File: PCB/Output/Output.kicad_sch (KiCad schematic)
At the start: 62 parts, among them J1 POWER, J10 O7, J11 O8, J12 O9, J13 O10, J2 Shelly, J2 USB-C, J4 O1, J5 O2, J6 O3, J7 O4, J8 O5, J9 O6, U1 MD8942, U2 ESP32-S3-MINI-1, U3 ISL89410, U4 ISL89410, U5 ISL89410, U6 ISL89410, U7 ISL89410

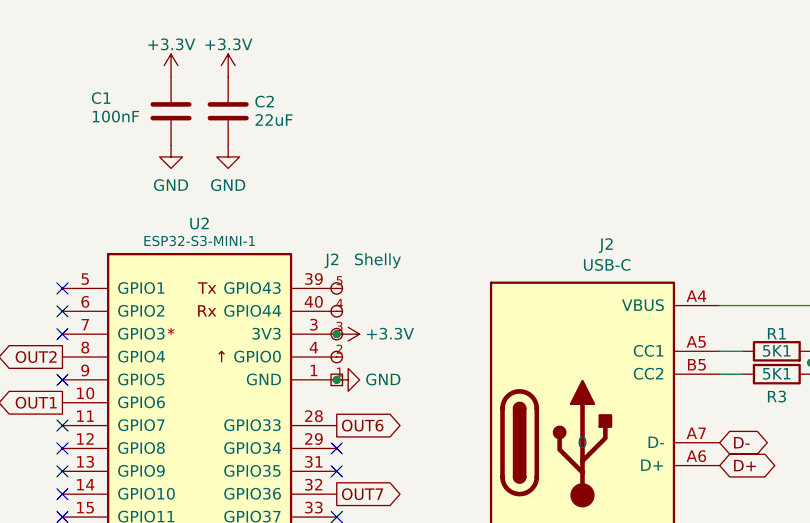
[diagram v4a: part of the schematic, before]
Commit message: Reworked boarder, and added simple LED on GPIO 0
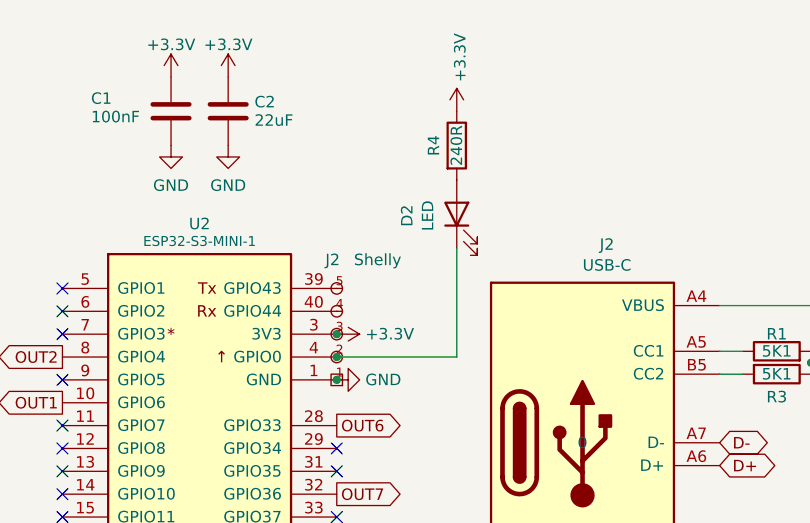
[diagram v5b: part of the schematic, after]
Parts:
- added D2: LED, LED_SMD:LED_0402_1005Metric, symbol Device:LED
- added R4: 240R, RevK:R_0402, symbol Device:R
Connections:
- net +3.3V: now also R4.1
- net at J2.2 (0), U2.4 (GPIO0): now also D2.1 (K)
- new net: D2.2 (A), R4.2
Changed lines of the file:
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@@
   (junction (at 95.885 87.63) (diameter 0) (color 0 0 0 0)
   )
+  (junction (at 68.58 55.245) (diameter 0) (color 0 0 0 0)
+  )
   (junction (at 68.58 57.785) (diameter 0) (color 0 0 0 0)
   )
@@
     (stroke (width 0) (type default))
   )
+  (wire (pts (xy 68.58 55.245) (xy 81.915 55.245))
+    (stroke (width 0) (type default))
+  )
   (wire (pts (xy 126.365 55.88) (xy 121.285 55.88))
     (stroke (width 0) (type default))
   )
+  (wire (pts (xy 81.915 55.245) (xy 81.915 43.18))
+    (stroke (width 0) (type default))
+  )
   (wire (pts (xy 111.125 54.61) (xy 113.665 54.61))
     (stroke (width 0) (type default))
@@
     )
   )
+  (symbol (lib_id "power:+3.3V") (at 81.915 27.94 0) (unit 1)
+    (in_bom yes) (on_board yes) (dnp no)
+    (property "Reference" "#PWR022" (at 81.915 31.75 0)
+      (effects (font (size 1.27 1.27)) hide)
+    )
+    (property "Value" "+3.3V" (at 82.296 24.6888 90)
+      (effects (font (size 1.27 1.27)) (justify left))
+    )
+    (property "Footprint" "" (at 81.915 27.94 0)
+      (effects (font (size 1.27 1.27)) hide)
+    )
+    (property "Datasheet" "" (at 81.915 27.94 0)
+      (effects (font (size 1.27 1.27)) hide)
+    )
+    (pin "1")
+    (instances
+      (project "GenericS3"
+        (path "/2d210a96-f81f-42a9-8bf4-1b43c11086f3"
+          (reference "#PWR022") (unit 1)
+        )
+      )
+      (project "Tas"
+        (path "/42713045-fffd-4b2d-ae1e-7232d705fb12"
+          (reference "#PWR021") (unit 1)
+        )
+      )
+      (project "Output"
+        (path "/770ad51a-7219-4633-b24a-bd20feb0a6c5"
+          (reference "#PWR083") (unit 1)
+        )
+      )
+    )
+  )
   (symbol (lib_id "power:GND") (at 48.895 177.165 180) (unit 1)
     (in_bom yes) (on_board yes) (dnp no) (fields_autoplaced)
@@
     )
   )
+  (symbol (lib_id "Device:LED") (at 81.915 39.37 90) (unit 1)
+    (in_bom yes) (on_board yes) (dnp no)
+    (property "Reference" "D2" (at 76.4032 39.5478 0)
+      (effects (font (size 1.27 1.27)))
+    )
+    (property "Value" "LED" (at 78.7146 39.5478 0)
+      (effects (font (size 1.27 1.27)))
+    )
+    (property "Footprint" "LED_SMD:LED_0402_1005Metric" (at 81.915 39.37 0)
+      (effects (font (size 1.27 1.27)) hide)
+    )
+    (property "Datasheet" "~" (at 81.915 39.37 0)
+      (effects (font (size 1.27 1.27)) hide)
+    )
+    (property "LCSC Part #" "C965790" (at 81.915 39.37 0)
+      (effects (font (size 1.27 1.27)) hide)
+    )
+    (pin "1")
+    (pin "2")
+    (instances
+      (project "GenericS3"
+        (path "/2d210a96-f81f-42a9-8bf4-1b43c11086f3"
+          (reference "D2") (unit 1)
+        )
+      )
+      (project "Tas"
+        (path "/42713045-fffd-4b2d-ae1e-7232d705fb12"
+          (reference "D3") (unit 1)
+        )
+      )
+      (project "Output"
+        (path "/770ad51a-7219-4633-b24a-bd20feb0a6c5"
+          (reference "D13") (unit 1)
+        )
+      )
+    )
+  )
   (symbol (lib_id "power:+3.3V") (at 79.375 184.785 180) (unit 1)
     (in_bom yes) (on_board yes) (dnp no) (fields_autoplaced)
@@
         )
       )
+    )
+  )
+  (symbol (lib_id "Device:R") (at 81.915 31.75 0) (unit 1)
+    (in_bom yes) (on_board yes) (dnp no)
+    (property "Reference" "R4" (at 79.375 31.75 90)
+      (effects (font (size 1.27 1.27)))
+    )
+    (property "Value" "240R" (at 81.915 31.75 90)
+      (effects (font (size 1.27 1.27)))
+    )
+    (property "Footprint" "RevK:R_0402" (at 80.137 31.75 90)
+      (effects (font (size 1.27 1.27)) hide)
+    )
+    (property "Datasheet" "~" (at 81.915 31.75 0)
+      (effects (font (size 1.27 1.27)) hide)
+    )
+    (pin "1")
+    (pin "2")
+    (instances
+      (project "GenericS3"
+        (path "/2d210a96-f81f-42a9-8bf4-1b43c11086f3"
+          (reference "R4") (unit 1)
+        )
+      )
+      (project "Tas"
+        (path "/42713045-fffd-4b2d-ae1e-7232d705fb12"
+          (reference "R5") (unit 1)
+        )
+      )
+      (project "Output"
+        (path "/770ad51a-7219-4633-b24a-bd20feb0a6c5"
+          (reference "R7") (unit 1)
+        )
+      )

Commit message: Library update
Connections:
- net +3.3V: now also D1.3 (-), D1.3 (-), D1.3 (-), D1.3 (-), D1.3 (-), D1.3 (-), D1.3 (-), D1.3 (-), D1.3 (-), D1.3 (-), D1.3 (-); no longer D1.2 (+), D1.2 (+), D1.2 (+), D1.2 (+), D1.2 (+), D1.2 (+), D1.2 (+), D1.2 (+), D1.2 (+), D1.2 (+), D1.2 (+)
- net GND: now also D1.2 (+), D1.2 (+), D1.2 (+), D1.2 (+), D1.2 (+), D1.2 (+), D1.2 (+), D1.2 (+), D1.2 (+), D1.2 (+), D1.2 (+); no longer D1.3 (⏚), D1.3 (⏚), D1.3 (⏚), D1.3 (⏚), D1.3 (⏚), D1.3 (⏚), D1.3 (⏚), D1.3 (⏚), D1.3 (⏚), D1.3 (⏚), D1.3 (⏚)
- net RGB renamed LED
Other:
- moved on the sheet: C3, R1
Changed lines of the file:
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@@
   (junction (at 68.58 52.705) (diameter 0) (color 0 0 0 0)
   )
-  (junction (at 79.375 102.235) (diameter 0) (color 0 0 0 0)
+  (junction (at 79.375 101.6) (diameter 0) (color 0 0 0 0)
   )
   (junction (at 121.285 55.88) (diameter 0) (color 0 0 0 0)
@@
   (no_connect (at 38.1 73.025))
   (no_connect (at 38.1 52.705))
-  (no_connect (at 38.1 102.235))
+  (no_connect (at 113.665 180.975))
   (no_connect (at 38.1 65.405))
   (no_connect (at 38.1 90.805))
@@
     (stroke (width 0) (type default))
   )
-  (wire (pts (xy 68.58 102.235) (xy 79.375 102.235))
+  (wire (pts (xy 68.58 101.6) (xy 79.375 101.6))
     (stroke (width 0) (type default))
   )
@@
     )
   )
-  (global_label "RGB" (shape input) (at 25.4 180.975 180) (fields_autoplaced)
+  (global_label "LED" (shape input) (at 25.4 180.975 180) (fields_autoplaced)
     (effects (font (size 1.27 1.27)) (justify right))
-    (property "Intersheetrefs" "${INTERSHEET_REFS}" (at 19.259 180.975 0)
+    (property "Intersheetrefs" "${INTERSHEET_REFS}" (at 19.6219 180.975 0)
       (effects (font (size 1.27 1.27)) (justify right) hide)
     )
@@
     )
   )
-  (global_label "RGB" (shape output) (at 38.1 88.265 180) (fields_autoplaced)
+  (global_label "LED" (shape output) (at 38.1 88.265 180) (fields_autoplaced)
     (effects (font (size 1.27 1.27)) (justify right))
-    (property "Intersheetrefs" "${INTERSHEET_REFS}" (at 31.959 88.265 0)
+    (property "Intersheetrefs" "${INTERSHEET_REFS}" (at 32.3219 88.265 0)
       (effects (font (size 1.27 1.27)) (justify right) hide)
     )
@@
       (effects (font (size 1.27 1.27)) hide)
     )
+    (property "Part No" "" (at 255.905 32.385 0)
+      (effects (font (size 1.27 1.27)) hide)
+    )
+    (property "Note" "" (at 255.905 32.385 0)
+      (effects (font (size 1.27 1.27)) hide)
+    )
     (pin "~")
     (instances
@@
       (effects (font (size 1.27 1.27)) hide)
     )
+    (property "Part No" "" (at 255.905 30.48 0)
+      (effects (font (size 1.27 1.27)) hide)
+    )
+    (property "Note" "" (at 255.905 30.48 0)
+      (effects (font (size 1.27 1.27)) hide)
+    )
     (pin "~")
     (instances
@@
     )
   )
-  (symbol (lib_id "Device:C") (at 79.375 106.045 0) (unit 1)
+  (symbol (lib_id "Device:C") (at 79.375 105.41 0) (unit 1)
     (in_bom yes) (on_board yes) (dnp no) (fields_autoplaced)
-    (property "Reference" "C3" (at 82.296 105.2103 0)
+    (property "Reference" "C3" (at 82.296 104.5753 0)
       (effects (font (size 1.27 1.27)) (justify left))
     )
-    (property "Value" "1uF" (at 82.296 107.7472 0)
+    (property "Value" "1uF" (at 82.296 107.1122 0)
       (effects (font (size 1.27 1.27)) (justify left))
     )
-    (property "Footprint" "RevK:C_0402" (at 80.3402 109.855 0)
+    (property "Footprint" "RevK:C_0402" (at 80.3402 109.22 0)
       (effects (font (size 1.27 1.27)) hide)
     )
-    (property "Datasheet" "~" (at 79.375 106.045 0)
+    (property "Datasheet" "~" (at 79.375 105.41 0)
       (effects (font (size 1.27 1.27)) hide)
     )
@@
       (effects (font (size 1.27 1.27)) hide)
     )
+    (property "Part No" "" (at 255.905 24.765 0)
+      (effects (font (size 1.27 1.27)) hide)
+    )
+    (property "Note" "" (at 255.905 24.765 0)
+      (effects (font (size 1.27 1.27)) hide)
+    )
     (pin "~")
     (instances
@@
       (effects (font (size 1.27 1.27)) hide)
     )
+    (property "Part No" "" (at 255.905 22.86 0)
+      (effects (font (size 1.27 1.27)) hide)
+    )
+    (property "Note" "" (at 255.905 22.86 0)
+      (effects (font (size 1.27 1.27)) hide)
+    )
     (pin "~")
     (instances
@@
       (effects (font (size 1.27 1.27)) hide)
     )
+    (property "Part No" "" (at 255.905 28.575 0)
+      (effects (font (size 1.27 1.27)) hide)
+    )
+    (property "Note" "" (at 255.905 28.575 0)
+      (effects (font (size 1.27 1.27)) hide)
+    )
     (pin "~")
     (instances
@@
     )
   )
-  (symbol (lib_id "power:+3.3V") (at 79.375 94.615 0) (unit 1)
+  (symbol (lib_id "power:+3.3V") (at 79.375 93.98 0) (unit 1)
     (in_bom yes) (on_board yes) (dnp no) (fields_autoplaced)
-    (property "Reference" "#PWR0106" (at 79.375 98.425 0)
+    (property "Reference" "#PWR0106" (at 79.375 97.79 0)
       (effects (font (size 1.27 1.27)) hide)
     )
-    (property "Value" "+3.3V" (at 79.375 91.0392 0)
+    (property "Value" "+3.3V" (at 79.375 90.4042 0)
       (effects (font (size 1.27 1.27)))
     )
-    (property "Footprint" "" (at 79.375 94.615 0)
+    (property "Footprint" "" (at 79.375 93.98 0)
       (effects (font (size 1.27 1.27)) hide)
     )
-    (property "Datasheet" "" (at 79.375 94.615 0)
+    (property "Datasheet" "" (at 79.375 93.98 0)
       (effects (font (size 1.27 1.27)) hide)
     )
@@
     )
   )
-  (symbol (lib_id "Device:R") (at 79.375 98.425 0) (unit 1)
+  (symbol (lib_id "Device:R") (at 79.375 97.79 0) (unit 1)
     (in_bom yes) (on_board yes) (dnp no)
-    (property "Reference" "R1" (at 81.28 98.425 90)
+    (property "Reference" "R1" (at 81.28 97.79 90)
       (effects (font (size 1.27 1.27)))
     )
-    (property "Value" "10K" (at 79.375 98.425 90)
+    (property "Value" "10K" (at 79.375 97.79 90)
       (effects (font (size 1.27 1.27)))
     )
-    (property "Footprint" "RevK:R_0402" (at 77.597 98.425 90)
+    (property "Footprint" "RevK:R_0402" (at 77.597 97.79 90)
       (effects (font (size 1.27 1.27)) hide)
     )
-    (property "Datasheet" "~" (at 79.375 98.425 0)
+    (property "Datasheet" "~" (at 79.375 97.79 0)
       (effects (font (size 1.27 1.27)) hide)
     )
@@
     )
   )
-  (symbol (lib_id "power:GND") (at 79.375 109.855 0) (unit 1)
+  (symbol (lib_id "power:GND") (at 79.375 109.22 0) (unit 1)
     (in_bom yes) (on_board yes) (dnp no) (fields_autoplaced)
-    (property "Reference" "#PWR0105" (at 79.375 116.205 0)
+    (property "Reference" "#PWR0105" (at 79.375 115.57 0)
       (effects (font (size 1.27 1.27)) hide)
     )
-    (property "Value" "GND" (at 79.375 114.2984 0)
+    (property "Value" "GND" (at 79.375 113.6634 0)
       (effects (font (size 1.27 1.27)))
     )
-    (property "Footprint" "" (at 79.375 109.855 0)
+    (property "Footprint" "" (at 79.375 109.22 0)
       (effects (font (size 1.27 1.27)) hide)
     )
-    (property "Datasheet" "" (at 79.375 109.855 0)
+    (property "Datasheet" "" (at 79.375 109.22 0)
       (effects (font (size 1.27 1.27)) hide)
     )
@@
       (effects (font (size 1.27 1.27)) hide)
     )
+    (property "Part No" "" (at 255.905 26.67 0)
+      (effects (font (size 1.27 1.27)) hide)
+    )
+    (property "Note" "" (at 255.905 26.67 0)
+      (effects (font (size 1.27 1.27)) hide)
+    )
     (pin "~")
     (instances
@@
       (effects (font (size 1.27 1.27)) hide)
     )
+    (property "Sim.Device" "D" (at 201.295 46.99 0)
+      (effects (font (size 1.27 1.27)) hide)
+    )
+    (property "Sim.Pins" "1=K 2=A" (at 201.295 46.99 0)
+      (effects (font (size 1.27 1.27)) hide)
+    )
     (pin "1")
     (pin "2")
@@
       (effects (font (size 1.27 1.27)) hide)
     )
+    (property "Part No" "" (at 255.905 34.29 0)
+      (effects (font (size 1.27 1.27)) hide)
+    )
+    (property "Note" "" (at 255.905 34.29 0)
+      (effects (font (size 1.27 1.27)) hide)
+    )
     (pin "~")
     (instances
@@
     )
   )
-  (symbol (lib_name "GND_1") (lib_id "power:GND") (at 68.58 57.785 90) (unit 1)
+  (symbol (lib_id "power:GND") (at 68.58 57.785 90) (unit 1)
     (in_bom yes) (on_board yes) (dnp no) (fields_autoplaced)
     (property "Reference" "#PWR01" (at 74.93 57.785 0)

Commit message: Tidy for order
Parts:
- removed AJK1: AJK, RevK:AJK, symbol RevK:AJK
- removed J2: USB-C, RevK:USC16-TR, symbol RevK:USB-C
- added C27: 100uF 6.3V, RevK:C_1206, symbol Device:C
- added J2: USB-C-Socket-V, RevK:USB-C-Socket-H, symbol RevK:USB-C-Socket-H
- added J4: USB-PROG, RevK:USB-PROG, symbol RevK:USB-PROG
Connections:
- net +3.3V: now also C1.2, C1.2, C1.2, C1.2, C1.2, C1.2, C1.2, C1.2, C1.2, C1.2, C1.2, D1.2 (+), D1.2 (+), D1.2 (+), D1.2 (+), D1.2 (+), D1.2 (+), D1.2 (+), D1.2 (+), D1.2 (+), D1.2 (+), D1.2 (+); no longer C1.1, C1.1, C1.1, C1.1, C1.1, C1.1, C1.1, C1.1, C1.1, C1.1, C1.1, D1.3 (-), D1.3 (-), D1.3 (-), D1.3 (-), D1.3 (-), D1.3 (-), D1.3 (-), D1.3 (-), D1.3 (-), D1.3 (-), D1.3 (-)
- net D+: now also J2.A6 (D+), J2.B6 (D+), J4.3 (D+)
- net D-: now also J2.A7 (D-), J2.B7 (D-), J4.2 (D-)
- net GND: now also C1.1, C1.1, C1.1, C1.1, C1.1, C1.1, C1.1, C1.1, C1.1, C1.1, C1.1, D1.3 (-), D1.3 (-), D1.3 (-), D1.3 (-), D1.3 (-), D1.3 (-), D1.3 (-), D1.3 (-), D1.3 (-), D1.3 (-), D1.3 (-), C27.1, J2.A1 (GND), J2.A12 (GND), J2.B1 (GND), J2.B12 (GND), J2.S1 (SHIELD), J4.4 (GND); no longer C1.2, C1.2, C1.2, C1.2, C1.2, C1.2, C1.2, C1.2, C1.2, C1.2, C1.2, D1.2 (+), D1.2 (+), D1.2 (+), D1.2 (+), D1.2 (+), D1.2 (+), D1.2 (+), D1.2 (+), D1.2 (+), D1.2 (+), D1.2 (+)
- net O1: now also U5.5 (OUT_B); no longer U3.7 (OUT_A)
- net O10: now also U5.7 (OUT_A); no longer U7.5 (OUT_B)
- net O2: now also U4.5 (OUT_B); no longer U3.5 (OUT_B)
- net O4: now also U3.5 (OUT_B); no longer U4.5 (OUT_B)
- net O5: now also U3.7 (OUT_A); no longer U5.5 (OUT_B)
- net O6: now also U7.5 (OUT_B); no longer U5.7 (OUT_A)
- net O7: now also U7.7 (OUT_A); no longer U6.7 (OUT_A)
- net O9: now also U6.7 (OUT_A); no longer U7.7 (OUT_A)
- net OUT1: now also U2.27 (GPIO47), U5.4 (IN_B); no longer U2.10 (GPIO6), U3.2 (IN_A)
- net OUT10: now also U2.28 (GPIO33), U5.2 (IN_A); no longer U2.37 (GPIO41), U7.4 (IN_B)
- net OUT2: now also U2.19 (GPIO15), U4.4 (IN_B); no longer U2.8 (GPIO4), U3.4 (IN_B)
- net OUT4: now also U2.8 (GPIO4), U3.4 (IN_B); no longer U2.19 (GPIO15), U4.4 (IN_B)
- net OUT5: now also U2.10 (GPIO6), U3.2 (IN_A); no longer U2.27 (GPIO47), U5.4 (IN_B)
- net OUT6: now also U2.37 (GPIO41), U7.4 (IN_B); no longer U2.28 (GPIO33), U5.2 (IN_A)
- net OUT7: now also U2.38 (GPIO42), U7.2 (IN_A); no longer U2.32 (GPIO36), U6.2 (IN_A)
- net OUT9: now also U2.32 (GPIO36), U6.2 (IN_A); no longer U2.38 (GPIO42), U7.2 (IN_A)
- net VBUS: now also C27.2, J2.A4 (VBUS), J2.A9 (VBUS), J2.B4 (VBUS), J2.B9 (VBUS), J4.1 (VBUS)
- net at R1.1: now also J2.A5 (CC1)
- net at R3.2: now also J2.B5 (CC2)
- net LED renamed RGB
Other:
- moved on the sheet: C1

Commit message: Library update
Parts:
- C1: value 10uF 50V -> 10uF 35V; LCSC Part # C1591 -> C194427
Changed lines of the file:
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@@
       (effects (font (size 1.27 1.27)) (justify left))
     )
-    (property "Value" "10uF 50V" (at 262.255 22.86 0)
+    (property "Value" "10uF 35V" (at 262.255 22.86 0)
       (effects (font (size 1.27 1.27)) (justify left))
     )
@@
       (effects (font (size 1.27 1.27)) hide)
     )
-    (property "LCSC Part #" "C1591" (at 255.905 22.86 0)
+    (property "LCSC Part #" "C194427" (at 255.905 22.86 0)
       (effects (font (size 1.27 1.27)) hide)
     )
